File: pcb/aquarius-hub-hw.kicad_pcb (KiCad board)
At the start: 4 copper layers, 50 x 50 mm, 164 parts, among them J1 XF2M-1415-1A, J10 BM08B-SRSS-TB, J11 BM04B-SRSS-TB, J13 SM04B-SRSS-TB, J14 BM03B-SRSS-TB, J2 USB_C_USB2.0_16P, J3 BM03B-SRSS-TB, J4 BM06B-SRSS-TB, J5 BM06B-SRSS-TB, J6 BM04B-SRSS-TB, J7 BM06B-SRSS-TB, J8 BM04B-SRSS-TB, J9 BM04B-SRSS-TB, Q1 MMBT2222A, SW1 EVQ-Q2B02W, SW2 EVQ-Q2B02W, U1 ESP32-S3-WROOM-1-N8R2, U2 LM66200DRLR, U3 USBLC6-2P6, U4 MCP23017T-E/ML, U6 LM66200DRLR, U7 AZ1084-3.3

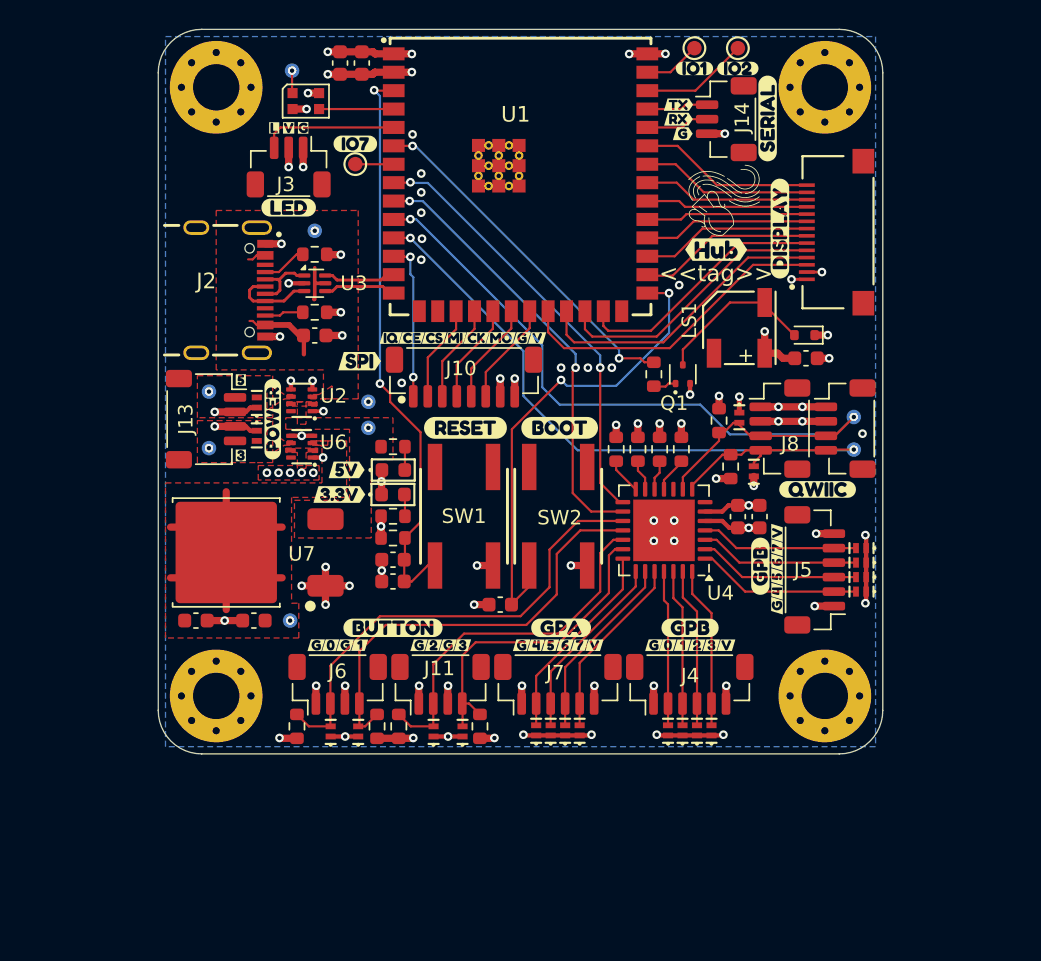
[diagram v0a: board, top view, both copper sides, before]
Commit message: Renamed peripherals to interfaces; added test points; added led jumper
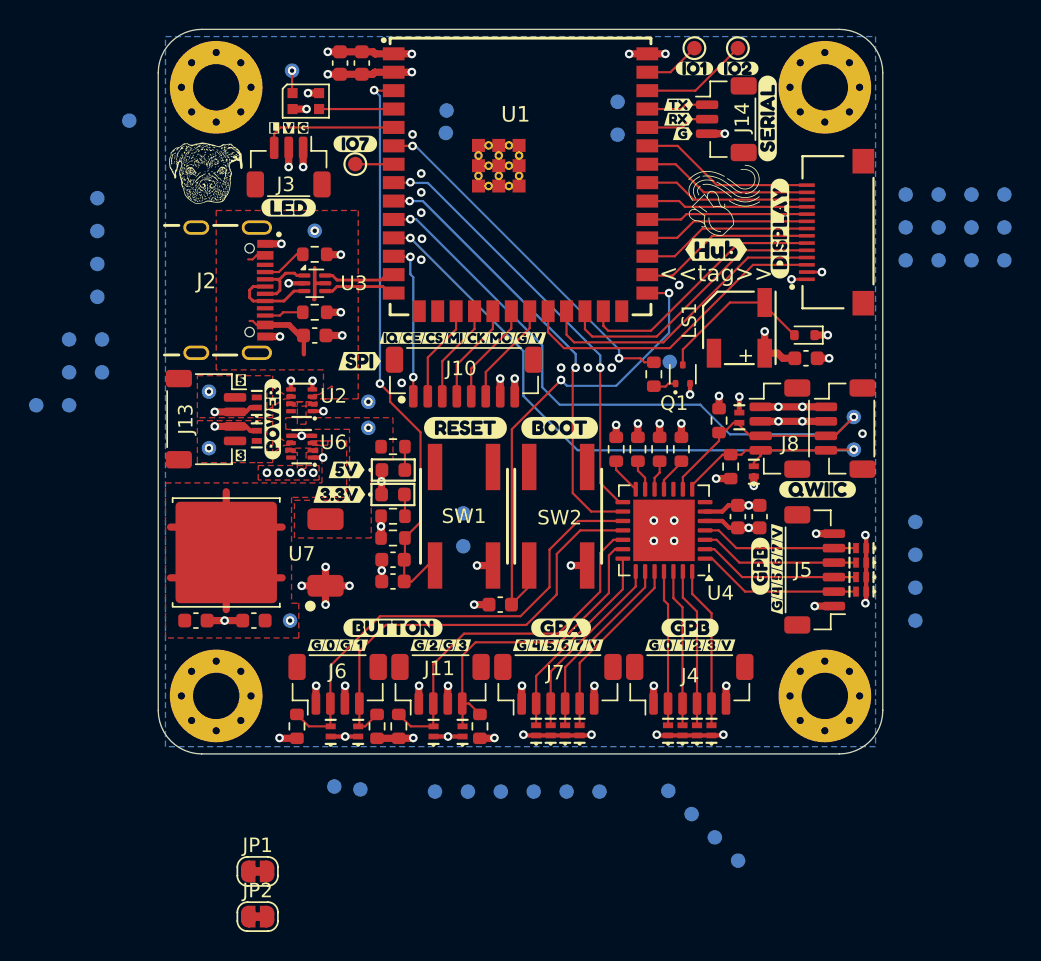
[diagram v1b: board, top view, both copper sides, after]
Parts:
- added JP1: ~, CRGM Connector:SolderJumper-2_P1.3mm_Bridged_RoundedPad1.0x1.5mm, F.Cu at (66.9, 108.1)
- added JP2: ~, CRGM Connector:SolderJumper-2_P1.3mm_Bridged_RoundedPad1.0x1.5mm, F.Cu at (66.9, 111.2)
- added REF**: Roxy 5mm, CRGM Logos:Roxy 5mm, F.Cu at (63.3, 59.9)
- added TP13: ~, CRGM Mechanical:TestPoint_Pad_D1.0mm, B.Cu at (111.6, 61.4)
- added TP14: ~, CRGM Mechanical:TestPoint_Pad_D1.0mm, B.Cu at (111.6, 63.7)
- added TP15: ~, CRGM Mechanical:TestPoint_Pad_D1.0mm, B.Cu at (111.6, 65.9)
- added TP16: ~, CRGM Mechanical:TestPoint_Pad_D1.0mm, B.Cu at (113.8, 61.4)
- added TP17: ~, CRGM Mechanical:TestPoint_Pad_D1.0mm, B.Cu at (113.8, 63.7)
- added TP18: ~, CRGM Mechanical:TestPoint_Pad_D1.0mm, B.Cu at (113.8, 65.9)
- added TP19: ~, CRGM Mechanical:TestPoint_Pad_D1.0mm, B.Cu at (116.1, 61.4)
- added TP20: ~, CRGM Mechanical:TestPoint_Pad_D1.0mm, B.Cu at (116.1, 63.7)
- added TP21: ~, CRGM Mechanical:TestPoint_Pad_D1.0mm, B.Cu at (116.1, 65.9)
- added TP22: ~, CRGM Mechanical:TestPoint_Pad_D1.0mm, B.Cu at (118.4, 61.4)
- added TP23: ~, CRGM Mechanical:TestPoint_Pad_D1.0mm, B.Cu at (118.4, 63.7)
- added TP24: ~, CRGM Mechanical:TestPoint_Pad_D1.0mm, B.Cu at (118.4, 65.9)
- added TP25: ~, CRGM Mechanical:TestPoint_Pad_D1.0mm, B.Cu at (55.8, 61.6)
- added TP26: ~, CRGM Mechanical:TestPoint_Pad_D1.0mm, B.Cu at (55.8, 63.9)
- added TP27: ~, CRGM Mechanical:TestPoint_Pad_D1.0mm, B.Cu at (55.8, 66.2)
- added TP28: ~, CRGM Mechanical:TestPoint_Pad_D1.0mm, B.Cu at (55.8, 68.5)
- added TP29: ~, CRGM Mechanical:TestPoint_Pad_D1.0mm, B.Cu at (91.7, 55.0)
- added TP30: ~, CRGM Mechanical:TestPoint_Pad_D1.0mm, B.Cu at (91.7, 57.3)
- added TP31: ~, CRGM Mechanical:TestPoint_Pad_D1.0mm, B.Cu at (51.6, 75.9)
- added TP32: ~, CRGM Mechanical:TestPoint_Pad_D1.0mm, B.Cu at (53.9, 71.4)
- added TP33: ~, CRGM Mechanical:TestPoint_Pad_D1.0mm, B.Cu at (53.9, 73.7)
- added TP34: ~, CRGM Mechanical:TestPoint_Pad_D1.0mm, B.Cu at (53.9, 75.9)
- added TP35: ~, CRGM Mechanical:TestPoint_Pad_D1.0mm, B.Cu at (56.1, 71.4)
- added TP36: ~, CRGM Mechanical:TestPoint_Pad_D1.0mm, B.Cu at (56.1, 73.7)
- added TP37: ~, CRGM Mechanical:TestPoint_Pad_D1.0mm, B.Cu at (79.9, 55.6)
- added TP38: ~, CRGM Mechanical:TestPoint_Pad_D1.0mm, B.Cu at (79.8, 57.1)
- added TP39: ~, CRGM Mechanical:TestPoint_Pad_D1.0mm, B.Cu at (58.0, 56.3)
- added TP40: ~, CRGM Mechanical:TestPoint_Pad_D1.0mm, B.Cu at (81.0, 83.4)
- added TP41: ~, CRGM Mechanical:TestPoint_Pad_D1.0mm, B.Cu at (81.0, 85.7)
- added TP42: ~, CRGM Mechanical:TestPoint_Pad_D1.0mm, B.Cu at (95.3, 73.0)
- added TP43: ~, CRGM Mechanical:TestPoint_Pad_D1.0mm, B.Cu at (95.2, 102.5)
- added TP44: ~, CRGM Mechanical:TestPoint_Pad_D1.0mm, B.Cu at (96.8, 104.2)
- added TP45: ~, CRGM Mechanical:TestPoint_Pad_D1.0mm, B.Cu at (98.4, 105.8)
- added TP46: ~, CRGM Mechanical:TestPoint_Pad_D1.0mm, B.Cu at (100.0, 107.4)
- added TP47: ~, CRGM Mechanical:TestPoint_Pad_D1.0mm, B.Cu at (112.2, 90.8)
- added TP48: ~, CRGM Mechanical:TestPoint_Pad_D1.0mm, B.Cu at (112.2, 88.5)
- added TP49: ~, CRGM Mechanical:TestPoint_Pad_D1.0mm, B.Cu at (112.2, 86.3)
- added TP50: ~, CRGM Mechanical:TestPoint_Pad_D1.0mm, B.Cu at (112.2, 84.0)
- added TP51: ~, CRGM Mechanical:TestPoint_Pad_D1.0mm, B.Cu at (72.2, 102.2)
- added TP52: ~, CRGM Mechanical:TestPoint_Pad_D1.0mm, B.Cu at (74.0, 102.5)
- added TP53: ~, CRGM Mechanical:TestPoint_Pad_D1.0mm, B.Cu at (79.1, 102.6)
- added TP54: ~, CRGM Mechanical:TestPoint_Pad_D1.0mm, B.Cu at (81.4, 102.6)
- added TP55: ~, CRGM Mechanical:TestPoint_Pad_D1.0mm, B.Cu at (83.6, 102.6)
- added TP56: ~, CRGM Mechanical:TestPoint_Pad_D1.0mm, B.Cu at (85.9, 102.6)
- added TP57: ~, CRGM Mechanical:TestPoint_Pad_D1.0mm, B.Cu at (88.2, 102.6)
- added TP58: ~, CRGM Mechanical:TestPoint_Pad_D1.0mm, B.Cu at (90.5, 102.6)
- D24: value Blue -> Orange
- H1, H2, H3, H4: value MountingHole_Pad -> ~
- TP1, TP10, TP11, TP12, TP2, TP3, TP4, TP5, TP6, TP7, TP8, TP9: value TP -> ~
- moved LOGO2 4.83 mm to (89.6, 63.6)
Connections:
- net /Peripherals/BUZZ_GND renamed /Interfaces/BUZZ_GND
- D23 pad 1: GND -> Net-(D23-K)
- D24 pad 1: GND -> Net-(D24-K)

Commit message: Adjusting for consistency
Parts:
- removed REF**: Roxy 5mm, CRGM Logos:Roxy 5mm
